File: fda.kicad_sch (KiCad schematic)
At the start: 59 parts, among them U706 OPA2197xD, U707 OPA2197xD, U73 OPA2388D, U74 THS4521IDGK

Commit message: Schematic complete, maybe
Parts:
- C720, C721: renamed from C?; footprint (none) -> Capacitor_SMD:C_0603_1608Metric; LCSC (none) -> C14858
- C722, C724: renamed from C?; footprint (none) -> Capacitor_SMD:C_0603_1608Metric; LCSC (none) -> C1664
- C723, C725, C726, C727: renamed from C?; footprint (none) -> Capacitor_SMD:C_0603_1608Metric; now left out of the parts list
- C728, C729, C730: renamed from C?; footprint (none) -> Capacitor_SMD:C_0603_1608Metric; LCSC (none) -> C307500
- C731: renamed from C?; value 0u33 -> 10n; footprint (none) -> Capacitor_SMD:C_0603_1608Metric; LCSC (none) -> C307500
- C732, C733, C734, C735, C736, C737: renamed from C?; footprint (none) -> Capacitor_SMD:C_0402_1005Metric; LCSC (none) -> C307331
- C738, C739: renamed from C?; value 0u1 -> 10n; footprint (none) -> Capacitor_SMD:C_0603_1608Metric; LCSC (none) -> C307500
- R734, R735: renamed from R?; footprint (none) -> Resistor_SMD:R_0402_1005Metric_Pad0.72x0.64mm_HandSolder; now left out of the parts list
- R752: renamed from R?; value 1k -> 3k3
- RN72, RN73: LCSC (none) -> C1358072; now left out of the parts list
- U706, U707: LCSC (none) -> C139363; now left out of the parts list
- U73: LCSC (none) -> C1517414
- U74: LCSC (none) -> C170157; now left out of the parts list
- gave numbers to parts that had none: 30
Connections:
- net In+ renamed IN+
- net In- renamed IN-

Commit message: Part selection
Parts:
- R720: footprint (none) -> Resistor_SMD:R_0603_1608Metric; LCSC (none) -> C21189
- R721, R722, R725, R726: footprint (none) -> Resistor_SMD:R_0603_1608Metric; LCSC (none) -> C23350
- R723, R724: footprint (none) -> Resistor_SMD:R_0603_1608Metric; LCSC (none) -> C22940
- R730, R731: footprint (none) -> Resistor_SMD:R_0402_1005Metric; LCSC (none) -> C25076
- R732, R733: footprint (none) -> Resistor_SMD:R_0603_1608Metric; LCSC (none) -> C22936
- R736, R743, R745, R751: footprint (none) -> Resistor_SMD:R_0603_1608Metric; LCSC (none) -> C23221
- R737, R742, R744, R750: footprint (none) -> Resistor_SMD:R_0402_1005Metric; LCSC (none) -> C25862
- R738, R741, R746, R749: footprint (none) -> Resistor_SMD:R_0402_1005Metric; LCSC (none) -> C25744
- R739, R740, R747, R748: footprint (none) -> Resistor_SMD:R_0402_1005Metric; LCSC (none) -> C25741
- R752: footprint (none) -> Resistor_SMD:R_0603_1608Metric; LCSC (none) -> C22978

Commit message: ERC passes.
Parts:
- C720, C721: value 100p -> 0n1
- C723, C726, C727: now not fitted
- R727, R728, R729: footprint (none) -> Resistor_SMD:R_0603_1608Metric; now left out of the parts list
- RN72, RN73: value 10k × 4 -> LT5400-1; footprint (none) -> Package_SO:MSOP-8-1EP_3x3mm_P0.65mm_EP1.68x1.88mm; symbol Device:R_Pack04 -> Parts:LT5400; R1 (none) -> 10k; R2 (none) -> 10k; R3 (none) -> 10k; R4 (none) -> 10k; now in the parts list
- U706, U707: value OPA2197xD -> OPA2197D
- U73: value OPA2388D -> OPA2388DGK; footprint Package_SO:SOIC-8_3.9x4.9mm_P1.27mm -> Package_SO:MSOP-8_3x3mm_P0.65mm; symbol Parts:OPA2388D -> Parts:OPA2388DGK; now left out of the parts list
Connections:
- net GNDPWR: now also RN72.9, RN73.9
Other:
- moved on the sheet: C720, C721, C722, C724, C725, C728, C729, C730, C731, C738, C739, R720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

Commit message: Everything assigned except for wierd shit.
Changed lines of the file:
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@@
 		)
 		(property "Value" "0u1"
-			(at 189.103 140.462 0)
+			(at 189.23 140.462 0)
 			(effects
 				(font
@@
 		)
 		(property "Value" "0u1"
-			(at 189.103 132.842 0)
+			(at 189.23 132.842 0)
 			(effects
 				(font
@@
 		)
 		(property "Value" "0u1"
-			(at 203.327 106.172 0)
+			(at 203.2 106.172 0)
 			(effects
 				(font
@@
 		)
 		(property "Value" "0u1"
-			(at 198.247 106.172 0)
+			(at 198.12 106.172 0)
 			(effects
 				(font
@@
 			)
 		)
-		(property "Datasheet" "50V"
+		(property "Datasheet" "C0G, 50V"
 			(at 55.88 99.06 0)
 			(effects
@@
 		(dnp no)
 		(property "Reference" "C720"
-			(at 120.65 87.122 90)
+			(at 119.888 93.472 90)
 			(effects
 				(font
 					(size 1.27 1.27)
 				)
-				(justify left)
 			)
 		)
 		(property "Value" "0n1"
-			(at 120.65 93.472 90)
+			(at 119.634 89.154 90)
 			(effects
 				(font
@@
 		(dnp no)
 		(property "Reference" "C739"
-			(at 134.874 158.242 0)
+			(at 134.62 158.242 0)
 			(effects
 				(font
@@
 		)
 		(property "Value" "10n"
-			(at 134.874 154.178 0)
+			(at 134.62 154.432 0)
 			(effects
 				(font
@@
 			)
 		)
-		(property "Datasheet" "50V"
+		(property "Datasheet" "C0G, 50V"
 			(at 80.01 111.76 0)
 			(effects
@@
 		(dnp no)
 		(property "Reference" "U73"
-			(at 191.77 104.14 0)
+			(at 191.77 104.394 0)
 			(effects
 				(font
@@
 		)
 		(property "Value" "OPA2388DGK"
-			(at 186.436 100.33 0)
+			(at 191.516 100.838 0)
 			(effects
 				(font
 					(size 1.27 1.27)
 				)
+				(justify right)
 			)
 		)
@@
 		(dnp no)
 		(property "Reference" "C731"
-			(at 104.394 154.432 0)
+			(at 104.14 154.432 0)
 			(effects
 				(font
@@
 		)
 		(property "Value" "10n"
-			(at 103.886 150.368 0)
+			(at 104.14 150.622 0)
 			(effects
 				(font
@@
 		)
 		(property "Value" "0n1"
-			(at 120.65 121.158 90)
+			(at 119.634 119.126 90)
 			(effects
 				(font
@@
 		)
 		(property "Value" "0u1"
-			(at 189.103 71.882 0)
+			(at 189.23 71.882 0)
 			(effects
 				(font
@@
 			)
 		)
-		(property "Datasheet" ""
+		(property "Datasheet" "~"
 			(at 87.63 107.95 0)
 			(effects
@@
 		)
 		(property "Value" "0u1"
-			(at 189.103 79.502 0)
+			(at 189.23 79.502 0)
 			(effects
 				(font
@@
 			)
 		)
-		(property "Datasheet" "C0G, 50V"
+		(property "Datasheet" "C0G"
 			(at 80.01 116.84 0)
 			(effects

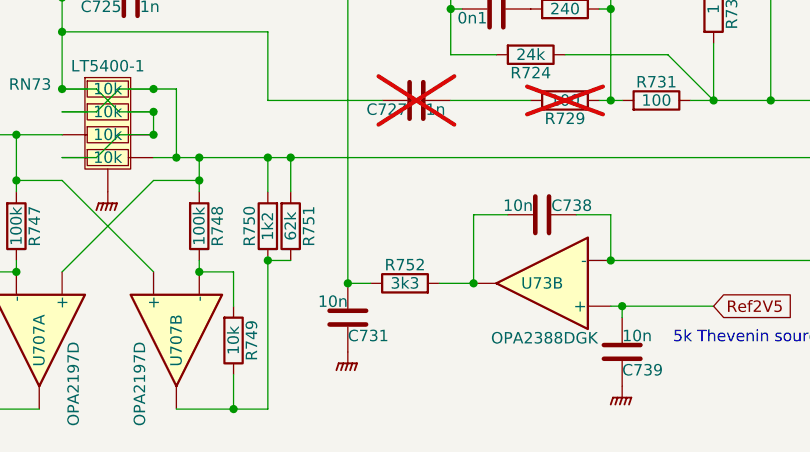
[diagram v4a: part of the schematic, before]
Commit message: Layout underway
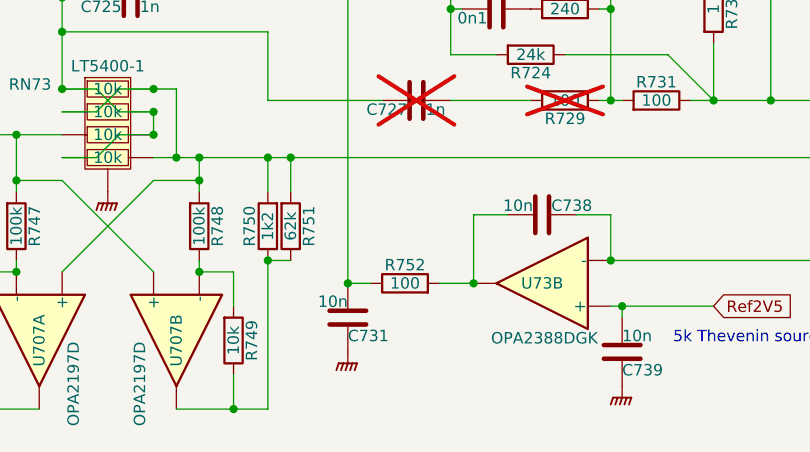
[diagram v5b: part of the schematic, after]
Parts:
- R752: value 3k3 -> 100; LCSC C22978 -> (none)
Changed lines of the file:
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@@
 			)
 		)
-		(property "Value" "3k3"
+		(property "Value" "100"
 			(at 110.49 148.59 90)
 			(effects
@@
 			)
 		)
-		(property "Datasheet" "0.1%, 10ppm/°C"
+		(property "Datasheet" "~"
 			(at 110.49 148.59 0)
 			(effects
@@
 			)
 		)
-		(property "LCSC" "C22978"
+		(property "LCSC" ""
 			(at 110.49 148.59 90)
 			(effects

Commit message: Whew.  DACs routed
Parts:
- added C741: 10u, Capacitor_SMD:C_0603_1608Metric, symbol Device:C
- added C742, C743, C744, C745: 0n1, Capacitor_SMD:C_0402_1005Metric, symbol Device:C
- added R732: 1, Resistor_SMD:R_0603_1608Metric, symbol Device:R
- added R753: 10k, Resistor_SMD:R_0402_1005Metric, symbol Device:R
- R752: LCSC (none) -> C23140
- R754: renamed from R732; value 1 -> 10k; footprint Resistor_SMD:R_0603_1608Metric -> Resistor_SMD:R_0402_1005Metric; LCSC C22936 -> C25744
- U706, U707: footprint Package_SO:SOIC-8_3.9x4.9mm_P1.27mm -> Parts:OPA2197; symbol Amplifier_Operational:OPA2197xD -> Parts:OPA2197D
- U73: footprint Package_SO:MSOP-8_3x3mm_P0.65mm -> Parts:OPA2388
- U74: footprint Package_SO:VSSOP-8_3x3mm_P0.65mm -> Parts:MSOP-8_3x3mm_P0.65mm
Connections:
- net +5VA: now also R754.2
- net GNDPWR: now also C741.2, R753.2
- net IN+: now also U706.3 (+); no longer U706.5 (+)
- net IN-: now also U707.3 (+); no longer U707.5 (+)
- net Out+: now also U707.5 (+); no longer U707.3 (+)
- net Out-: now also U706.5 (+), R732.1; no longer R754.2, U706.3 (+)
- net at R736.1, R737.1, R738.1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: now also C742.1
- net at R744.1, R745.1, U707.1: now also R746.2, C743.2; no longer R746.1
- net at R750.1, R751.1, U707.7: now also R749.2, C745.2; no longer R749.1
- net at R741.1, R742.1, R743.1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: now also C744.1
- net at R741.2, U706.6 (-): now also R739.1, C744.2; no longer R740.1
- net at R738.2, U706.2 (-): now also R740.1, C742.2; no longer R739.1
- net at C731.1, R752.1, U74.2 (V_{OCM}): no longer R722.2
- net at C728.1: now also R732.2; no longer R754.1
- new net: C743.1, R746.1, R748.1, U707.2 (-)
- new net: C745.1, R747.1, R749.1, U707.6 (-)
- new net: C741.1, R722.2, R753.1, R754.1
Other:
- moved on the sheet: R736, R737, R738, R739, R740, R741, R742, R743, R744, R745, R746, R747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

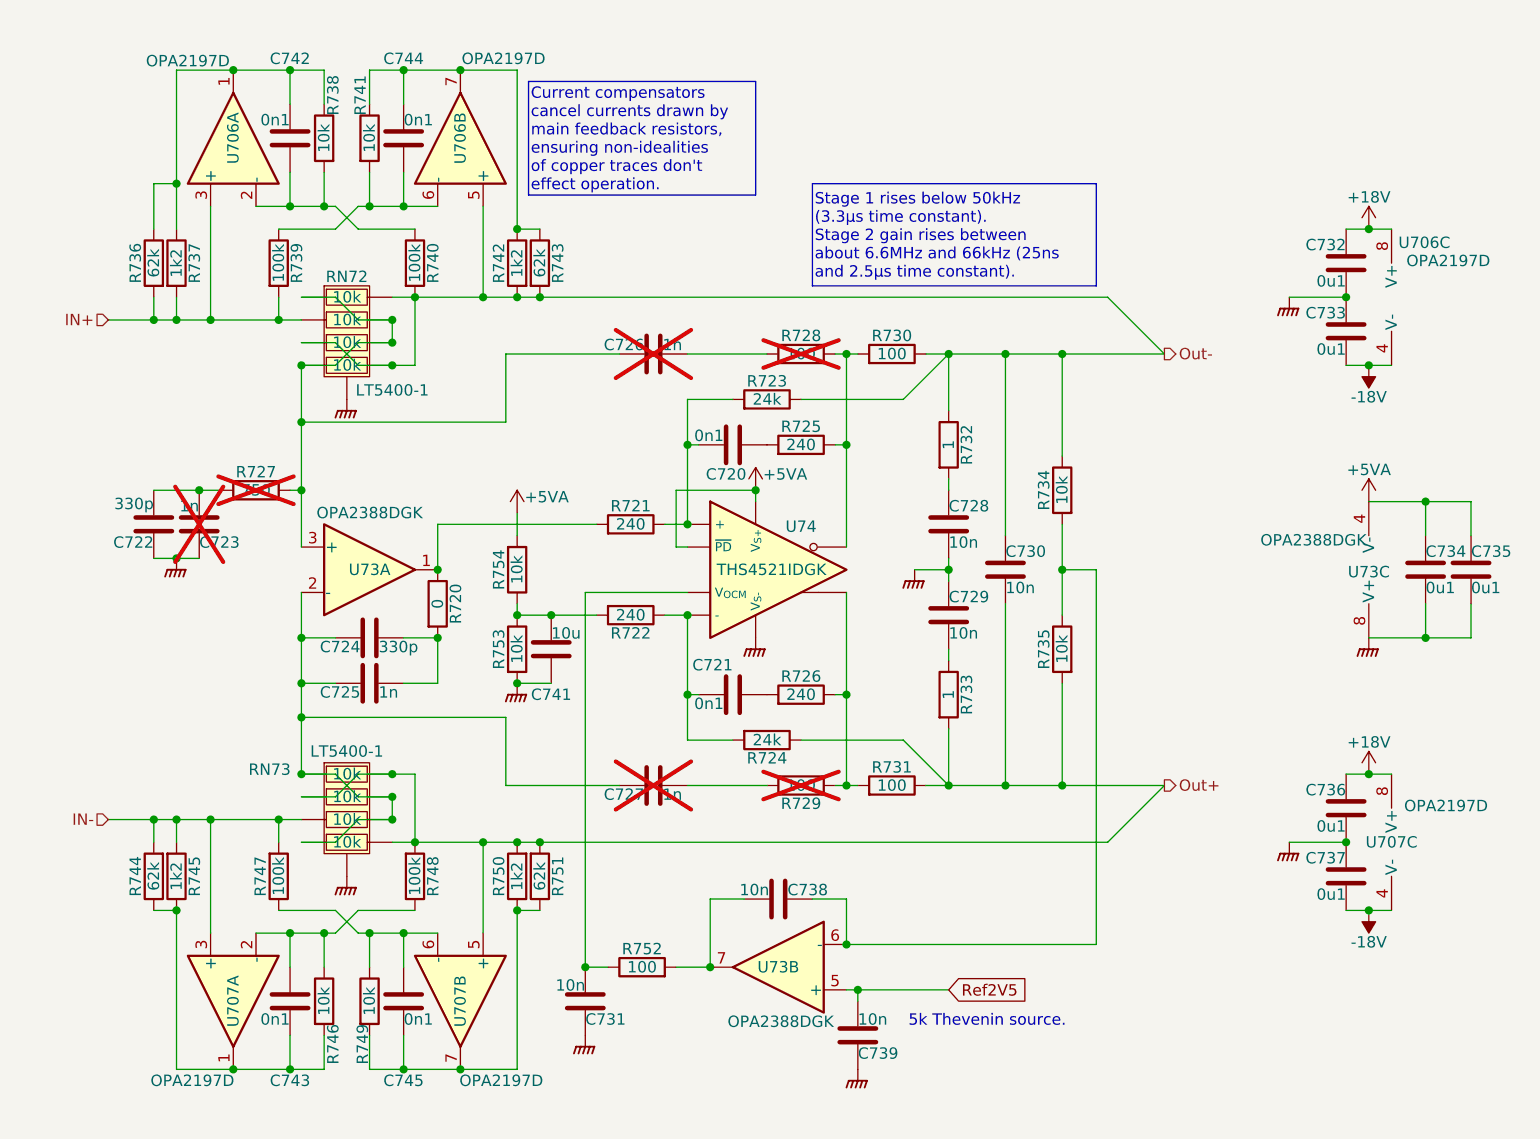
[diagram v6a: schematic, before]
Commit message: Tweaks following spice simulation.
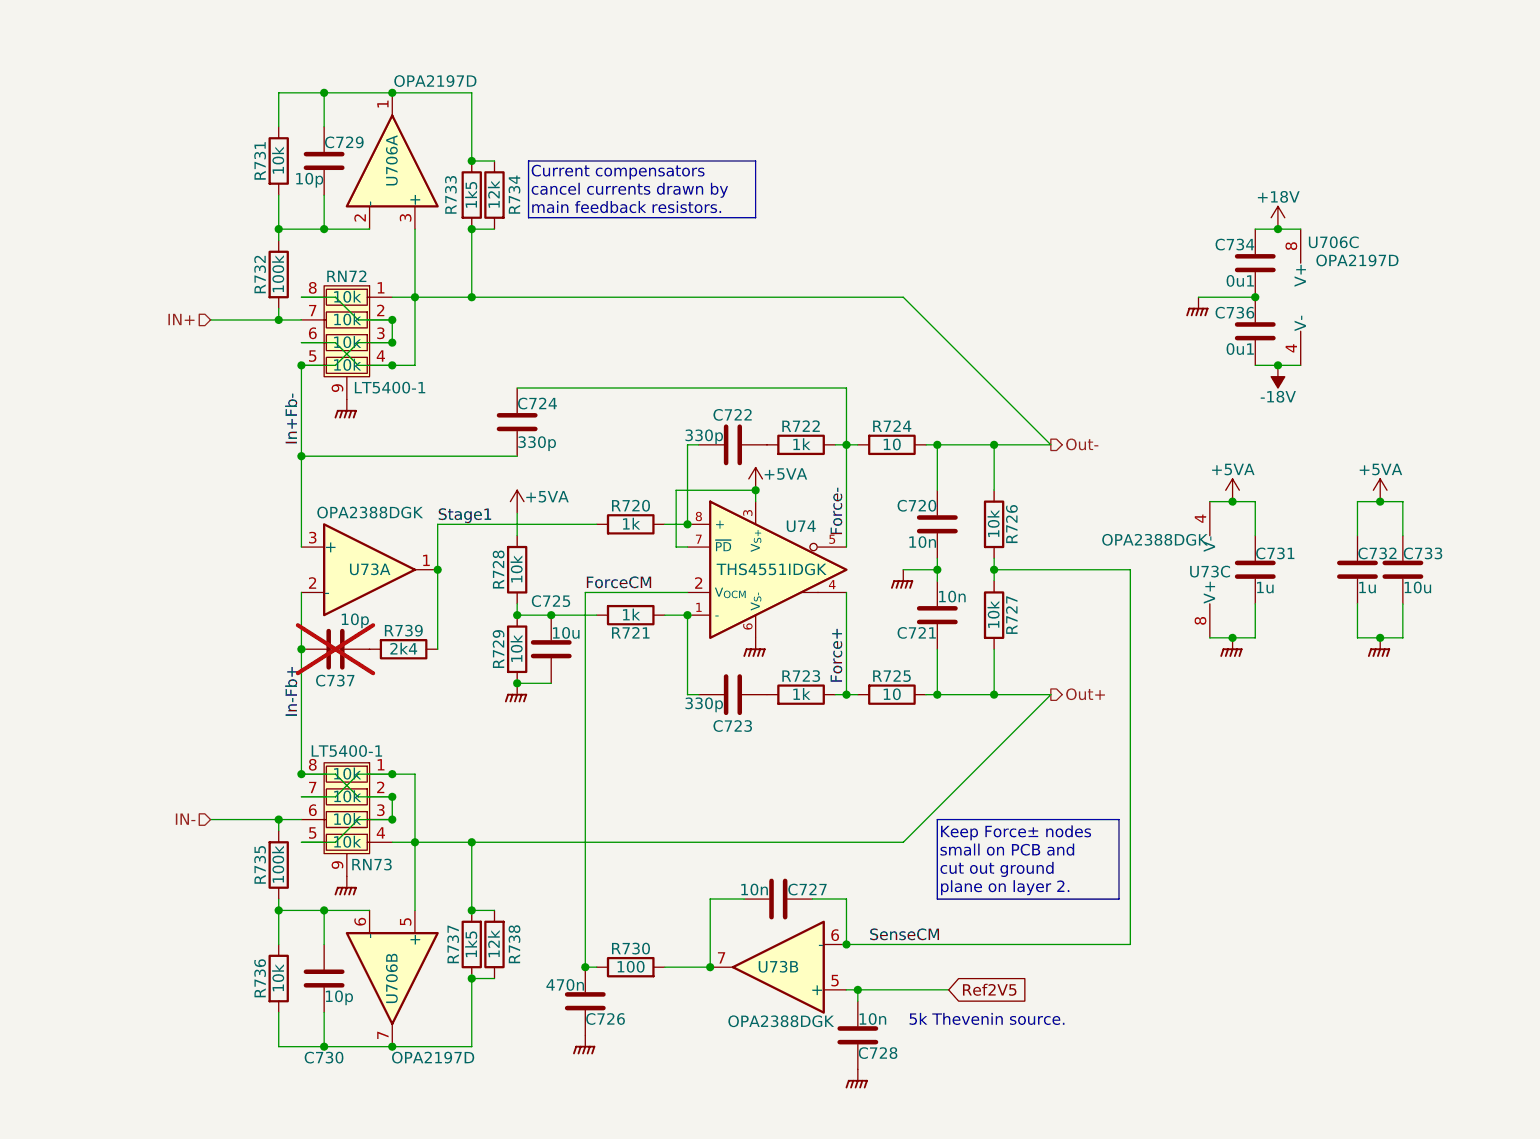
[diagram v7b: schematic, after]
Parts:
- removed C735, C737: 0u1, Capacitor_SMD:C_0402_1005Metric, symbol Device:C
- removed C738, C739: 10n, Capacitor_SMD:C_0603_1608Metric, symbol Device:C
- removed C741: 10u, Capacitor_SMD:C_0603_1608Metric, symbol Device:C
- removed C742, C743, C744, C745: 0n1, Capacitor_SMD:C_0402_1005Metric, symbol Device:C
- removed R740, R747, R748: 100k, Resistor_SMD:R_0402_1005Metric, symbol Device:R
- removed R741, R746, R749, R753, R754: 10k, Resistor_SMD:R_0402_1005Metric, symbol Device:R
- removed R742, R744, R750: 1k2, Resistor_SMD:R_0402_1005Metric, symbol Device:R
- removed R743, R745, R751: 62k, Resistor_SMD:R_0603_1608Metric, symbol Device:R
- removed R752: 100, Resistor_SMD:R_0603_1608Metric, symbol Device:R
- removed U707: OPA2197D, Parts:OPA2197, symbol Parts:OPA2197D
- added C724: 330p, Capacitor_SMD:C_0603_1608Metric, symbol Device:C
- C720, C721: value 0n1 -> 10n; LCSC C14858 -> (none); now left out of the parts list
- C723: value 1n -> 330p; LCSC (none) -> C1664; now fitted; now in the parts list
- C725: value 1n -> 10u; LCSC (none) -> C96446; now in the parts list
- C726: value 1n -> 470n; footprint Capacitor_SMD:C_0603_1608Metric -> Capacitor_SMD:C_0402_1005Metric; LCSC (none) -> C47339; now fitted; now in the parts list
- C727: value 1n -> 10n; LCSC (none) -> C307500; now fitted; now in the parts list
- C729, C730: value 10n -> 10p; footprint Capacitor_SMD:C_0603_1608Metric -> Capacitor_SMD:C_0402_1005Metric; LCSC C307500 -> C1546?
- C731: value 10n -> 1u; footprint Capacitor_SMD:C_0603_1608Metric -> Capacitor_SMD:C_0402_1005Metric; LCSC C307500 -> C52923
- C732: value 0u1 -> 1u; LCSC C307331 -> C52923
- C733: value 0u1 -> 10u; footprint Capacitor_SMD:C_0402_1005Metric -> Capacitor_SMD:C_0603_1608Metric; LCSC C307331 -> C96446
- C737: renamed from C724; value 330p -> 10p; LCSC C1664 -> (none); now not fitted; now left out of the parts list
- R720: value 0 -> 1k; footprint Resistor_SMD:R_0603_1608Metric -> Capacitor_SMD:C_0402_1005Metric; LCSC C21189 -> C11702
- R721: value 240 -> 1k; footprint Resistor_SMD:R_0603_1608Metric -> Capacitor_SMD:C_0402_1005Metric; LCSC C23350 -> C11702
- R722: value 240 -> 1k; footprint Resistor_SMD:R_0603_1608Metric -> Capacitor_SMD:C_0603_1608Metric; LCSC C23350 -> C22765
- R723: value 24k -> 1k; footprint Resistor_SMD:R_0603_1608Metric -> Capacitor_SMD:C_0603_1608Metric; LCSC C22940 -> C22765
- R724: value 24k -> 10; footprint Resistor_SMD:R_0603_1608Metric -> Resistor_SMD:R_0402_1005Metric; LCSC C22940 -> C25077
- R725: value 240 -> 10; footprint Resistor_SMD:R_0603_1608Metric -> Resistor_SMD:R_0402_1005Metric; LCSC C23350 -> C25077
- R726: value 240 -> 10k; LCSC C23350 -> (none); now left out of the parts list
- R727: value 750 -> 10k; now fitted
- R728, R729: value 100 -> 10k; footprint Resistor_SMD:R_0603_1608Metric -> Resistor_SMD:R_0402_1005Metric; LCSC (none) -> C25744; now fitted; now in the parts list
- R731: value 100 -> 10k; LCSC C25076 -> C25744
- R732: value 1 -> 100k; footprint Resistor_SMD:R_0603_1608Metric -> Resistor_SMD:R_0402_1005Metric; LCSC C22936 -> C25741
- R733: value 1 -> 1k5; footprint Resistor_SMD:R_0603_1608Metric -> Resistor_SMD:R_0402_1005Metric; LCSC C22936 -> C25867
- R734: value 10k -> 12k; footprint Resistor_SMD:R_0402_1005Metric_Pad0.72x0.64mm_HandSolder -> Resistor_SMD:R_0603_1608Metric; LCSC (none) -> C22790; now in the parts list
- R735: value 10k -> 100k; footprint Resistor_SMD:R_0402_1005Metric_Pad0.72x0.64mm_HandSolder -> Resistor_SMD:R_0402_1005Metric; LCSC (none) -> C25741; now in the parts list
- R736: value 62k -> 10k; footprint Resistor_SMD:R_0603_1608Metric -> Resistor_SMD:R_0402_1005Metric; LCSC C23221 -> C25744
- R737: value 1k2 -> 1k5; LCSC C25862 -> C25867
- R738: value 10k -> 12k; footprint Resistor_SMD:R_0402_1005Metric -> Resistor_SMD:R_0603_1608Metric; LCSC C25744 -> C22790
- R739: value 100k -> 2k4; footprint Resistor_SMD:R_0402_1005Metric -> Resistor_SMD:R_0603_1608Metric; LCSC C25741 -> C22940
- RN72, RN73: footprint Package_SO:MSOP-8-1EP_3x3mm_P0.65mm_EP1.68x1.88mm -> Parts:MSOP-8-1EP_3x3mm_P0.65mm_EP1.68x1.88mm
- U74: value THS4521IDGK -> THS4551IDGK; footprint Parts:MSOP-8_3x3mm_P0.65mm -> Parts:OPA4521
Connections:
- net +18V: now also C734.1; no longer C732.1, C736.1
- net +5VA: now also C731.1, C732.1, C733.1, R728.2; no longer C734.1
- net -18V: now also C736.2; no longer C733.2
- net GNDPWR: now also C720.2, C721.1, C725.2, C726.2, C733.2, C736.1, R729.2; no longer C722.2, C723.2, C729.2, C733.1, C736.2
- net IN+: now also R732.2, RN72.7; no longer R736.2, R737.2, R739.2, RN72.2, U706.3 (+)
- net IN-: now also R735.2, RN73.6; no longer RN73.3
- net Out+: now also C721.2, R725.1, R727.2, R737.2, R738.2, RN73.1, RN73.4, RN73.7, U706.5 (+); no longer C730.2, R724.1, R731.1, R733.2, R735.2, RN73.2, RN73.5, RN73.8
- net Out-: now also C720.1, R724.1, R726.1, R733.2, R734.2, RN72.1, RN72.4, RN72.6, U706.3 (+); no longer C730.1, R723.1, R730.1, R732.1, R734.1, RN72.3, RN72.5, RN72.8, U706.5 (+)
- net Ref2V5: now also C728.1
- net at R737.1, R738.1: now also C730.2, R736.2, U706.7; no longer R736.1, U706.1
- net at U73.7: now also C727.1, R730.2
- net at U706.6 (-): now also C730.1, R735.1, R736.1; no longer R739.1
- net at U706.2 (-): now also C729.2, R731.2, R732.1; no longer R738.2
- net at C729.1, R733.1: now also R731.1, R734.1, U706.1
- net Force+: now reaches R725.2
- net Force+: now also R723.1, U74.4; no longer C720.2
- net Force-: now reaches R722.1, R724.2
- net Force-: now also U74.5, C724.2; no longer C721.2, U74.1 (-)
- net ForceCM: now reaches C726.1
- net ForceCM: now also R730.1, U74.2 (V_{OCM}); no longer R728.2
- net SenseCM: now reaches R726.2
- net SenseCM: now also C727.2, R727.1, U73.6 (-); no longer C721.1
- net at R722.2: now also C722.2
- new net: C723.1, R723.2
- new net: C737.1, R739.2
- new net: C722.1, R720.1, U74.8 (+)
- new net: C725.1, R721.2, R728.1, R729.1
- new net: C723.2, R721.1, U74.1 (-)
- new net In+Fb-: C724.1, RN72.2, RN72.3, RN72.5, RN72.8, U73.3 (+)
- new net In-Fb+: C737.2, RN73.2, RN73.3, RN73.5, RN73.8, U73.2 (-)
- new net Stage1: R720.2, R739.1, U73.1
